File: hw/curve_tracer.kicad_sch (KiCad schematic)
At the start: 10 parts, among them J101 9V Supply, SW101 SW_Push, U101 MCU_Nucleo_L432KC

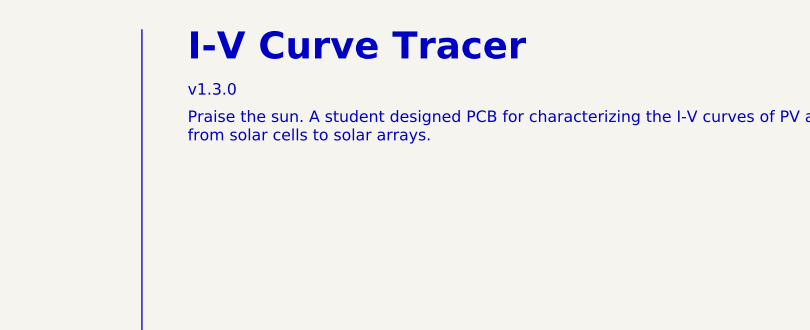
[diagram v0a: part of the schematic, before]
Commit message: reorg project directory, moved in fw files
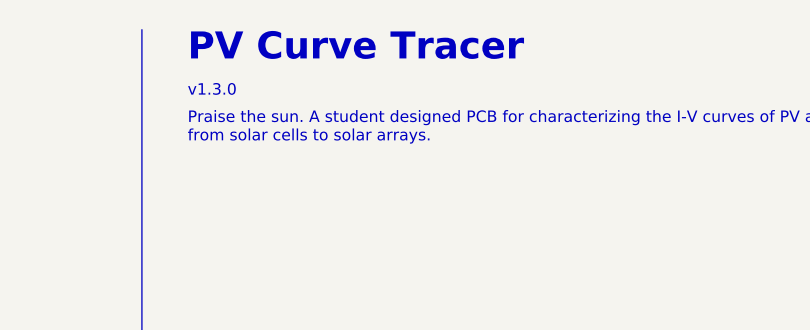
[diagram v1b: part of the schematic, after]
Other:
- note added: "PV Curve Tracer"
- note removed: "I-V Curve Tracer"
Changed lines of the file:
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@@
     (effects (font (size 1.27 1.27)) (justify left bottom))
   )
-  (text "I-V Curve Tracer" (at 177.8 29.21 0)
+  (text "PV Curve Tracer" (at 177.8 29.21 0)
     (effects (font (size 3 3) (thickness 0.6) bold) (justify left bottom))
   )
@@
     )
     (instances
-      (project "IV Curve Tracer"
+      (project "curve_tracer"
         (path "/4c8027f3-915c-4853-a53c-bc426a9ca6f1"
           (reference "H101") (unit 1)
@@
     )
     (instances
-      (project "IV Curve Tracer"
+      (project "curve_tracer"
         (path "/4c8027f3-915c-4853-a53c-bc426a9ca6f1"
           (reference "H102") (unit 1)
@@
     (pin "9")
     (instances
-      (project "IV Curve Tracer"
+      (project "curve_tracer"
         (path "/4c8027f3-915c-4853-a53c-bc426a9ca6f1"
           (reference "U101") (unit 1)
@@
     (pin "2")
     (instances
-      (project "IV Curve Tracer"
+      (project "curve_tracer"
         (path "/4c8027f3-915c-4853-a53c-bc426a9ca6f1"
           (reference "C101") (unit 1)
@@
     (pin "2")
     (instances
-      (project "IV Curve Tracer"
+      (project "curve_tracer"
         (path "/4c8027f3-915c-4853-a53c-bc426a9ca6f1"
           (reference "SW101") (unit 1)
@@
     (pin "2")
     (instances
-      (project "IV Curve Tracer"
+      (project "curve_tracer"
         (path "/4c8027f3-915c-4853-a53c-bc426a9ca6f1"
           (reference "J101") (unit 1)
@@
     (pin "1")
     (instances
-      (project "IV Curve Tracer"
+      (project "curve_tracer"
         (path "/4c8027f3-915c-4853-a53c-bc426a9ca6f1"
           (reference "TP103") (unit 1)
@@
     (pin "1")
     (instances
-      (project "IV Curve Tracer"
+      (project "curve_tracer"
         (path "/4c8027f3-915c-4853-a53c-bc426a9ca6f1"
           (reference "#PWR0101") (unit 1)
@@
     )
     (instances
-      (project "IV Curve Tracer"
+      (project "curve_tracer"
         (path "/4c8027f3-915c-4853-a53c-bc426a9ca6f1"
           (reference "H103") (unit 1)
@@
     (pin "1")
     (instances
-      (project "IV Curve Tracer"
+      (project "curve_tracer"
         (path "/4c8027f3-915c-4853-a53c-bc426a9ca6f1"
           (reference "TP101") (unit 1)
@@
     (pin "1")
     (instances
-      (project "IV Curve Tracer"
+      (project "curve_tracer"
         (path "/4c8027f3-915c-4853-a53c-bc426a9ca6f1"
           (reference "#PWR0107") (unit 1)
@@
     (pin "1")
     (instances
-      (project "IV Curve Tracer"
+      (project "curve_tracer"
         (path "/4c8027f3-915c-4853-a53c-bc426a9ca6f1"
           (reference "#PWR0106") (unit 1)
@@
     (pin "1")
     (instances
-      (project "IV Curve Tracer"
+      (project "curve_tracer"
         (path "/4c8027f3-915c-4853-a53c-bc426a9ca6f1"
           (reference "#PWR0102") (unit 1)
@@
     (pin "1")
     (instances
-      (project "IV Curve Tracer"
+      (project "curve_tracer"
         (path "/4c8027f3-915c-4853-a53c-bc426a9ca6f1"
           (reference "TP102") (unit 1)
@@
     (pin "1")
     (instances
-      (project "IV Curve Tracer"
+      (project "curve_tracer"
         (path "/4c8027f3-915c-4853-a53c-bc426a9ca6f1"
           (reference "#PWR0105") (unit 1)
@@
     )
     (instances
-      (project "IV Curve Tracer"
+      (project "curve_tracer"
         (path "/4c8027f3-915c-4853-a53c-bc426a9ca6f1" (page "6"))
       )
@@
     )
     (instances
-      (project "IV Curve Tracer"
+      (project "curve_tracer"
         (path "/4c8027f3-915c-4853-a53c-bc426a9ca6f1" (page "3"))
       )
@@
     )
     (instances
-      (project "IV Curve Tracer"
+      (project "curve_tracer"
         (path "/4c8027f3-915c-4853-a53c-bc426a9ca6f1" (page "2"))
       )
@@
     )
     (instances
-      (project "IV Curve Tracer"
+      (project "curve_tracer"
         (path "/4c8027f3-915c-4853-a53c-bc426a9ca6f1" (page "4"))
       )
@@
     )
     (instances
-      (project "IV Curve Tracer"
+      (project "curve_tracer"
         (path "/4c8027f3-915c-4853-a53c-bc426a9ca6f1" (page "5"))
       )
